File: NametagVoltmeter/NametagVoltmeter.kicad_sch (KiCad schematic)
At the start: 61 parts, among them J1 Conn_01x07_Pin, J11 I_Input, J12 Conn_01x02_Pin, J14 Barrel_Jack, J15 Barrel_Jack, J16 Conn_01x01_Socket, J17 Conn_01x01_Socket, J2 MicoSD, J3 Conn_01x07_Pin, J7 Conn_01x02_Pin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

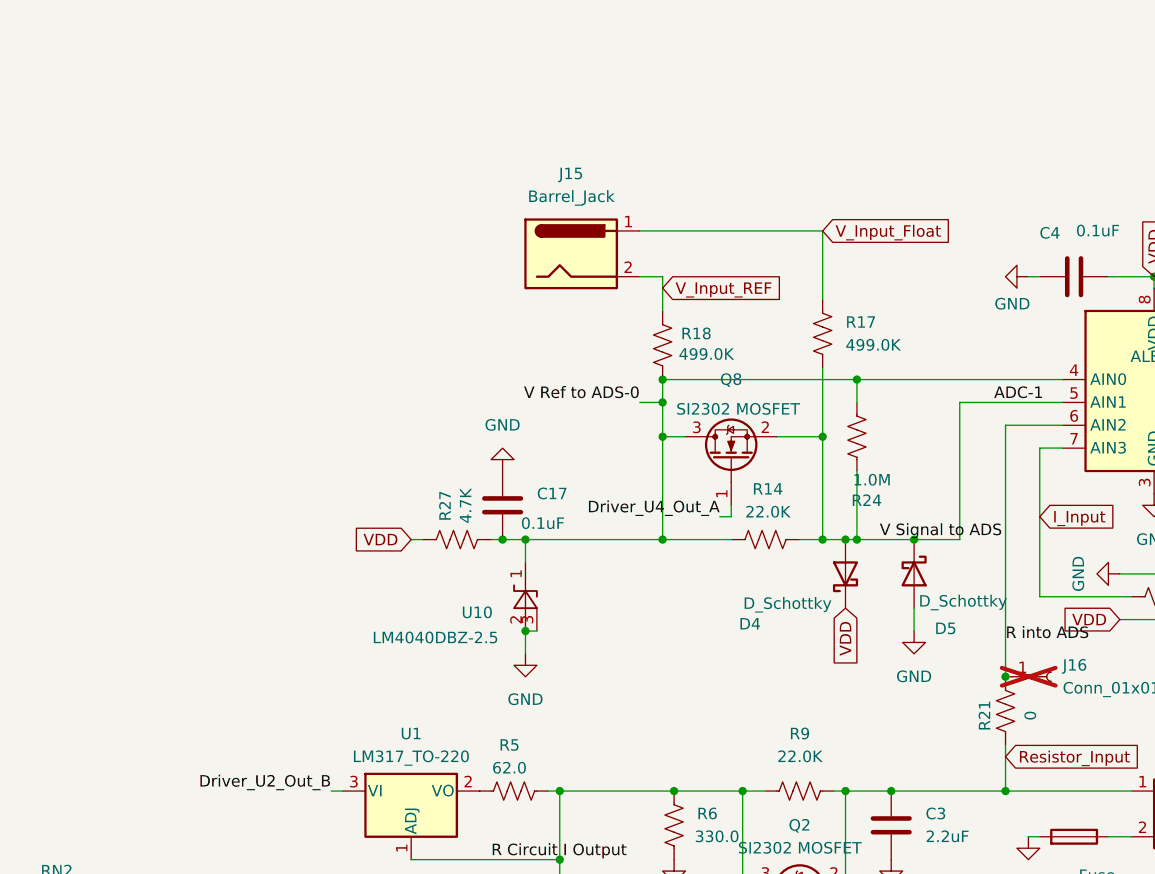
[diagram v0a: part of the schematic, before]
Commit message: Making a Version of Code for Newest PCB Revision
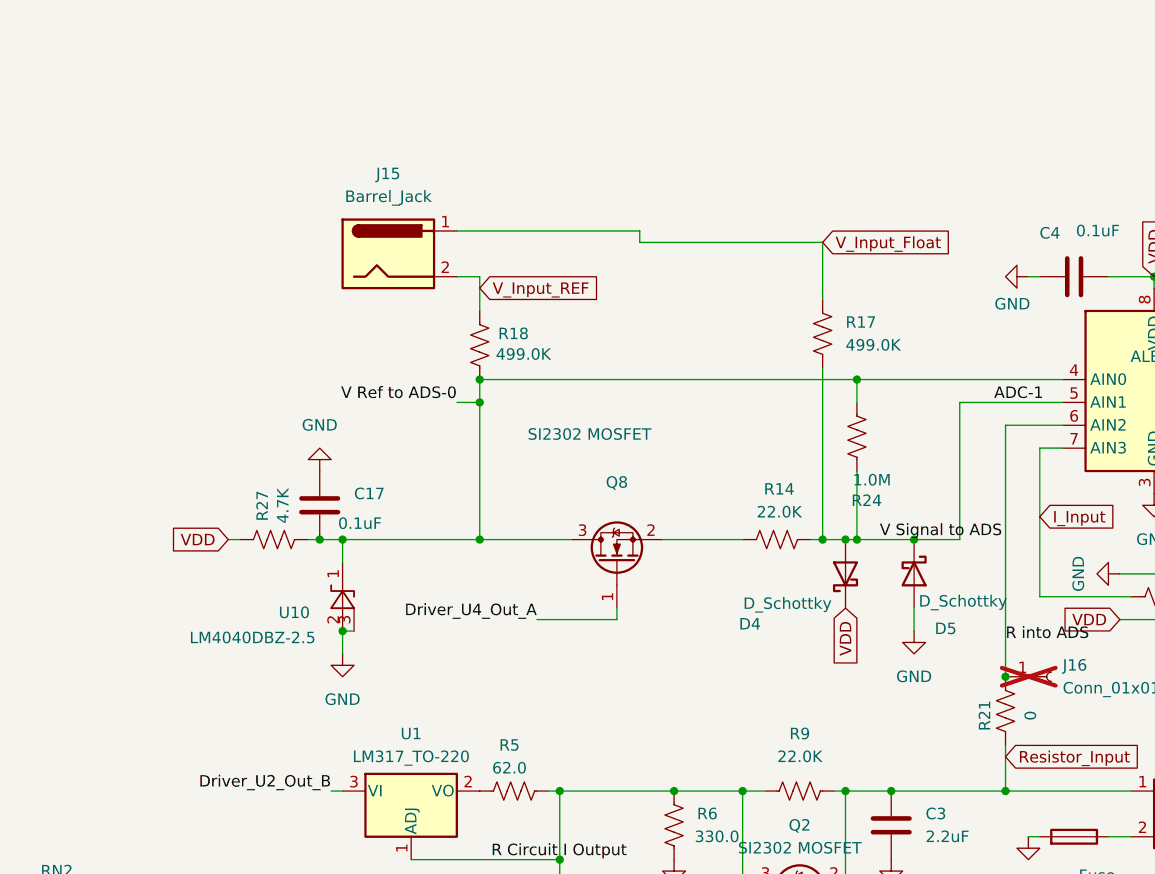
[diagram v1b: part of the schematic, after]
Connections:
- net ADC-1: no longer Q8.2 (S)
- net V Ref to ADS-0: no longer R14.1
- new net: Q8.2 (S), R14.1
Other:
- moved on the sheet: C17, J15, Q8, R14, R18, R27, U10

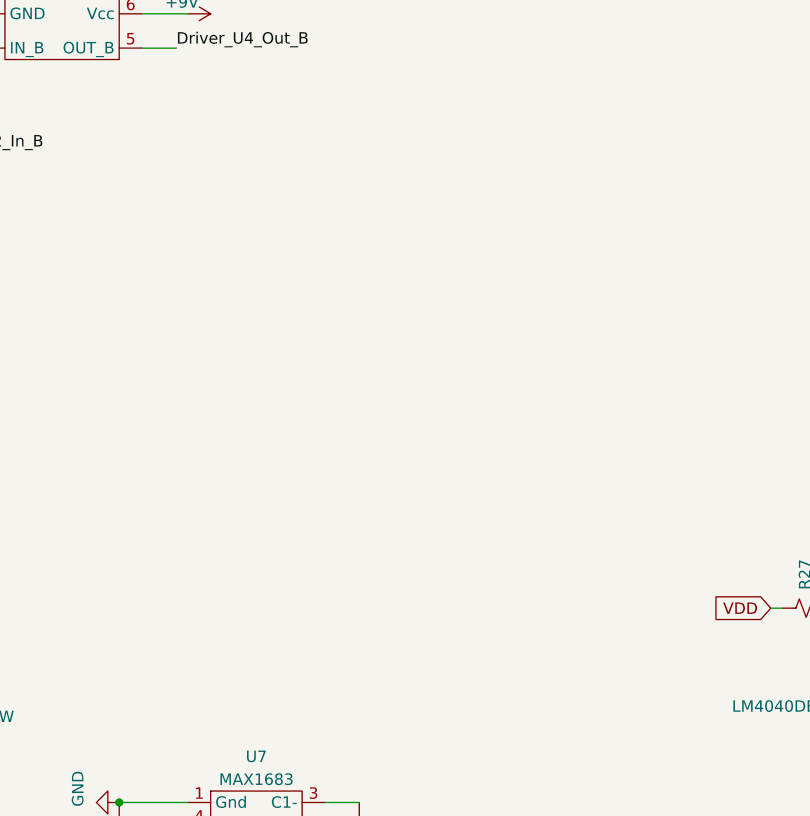
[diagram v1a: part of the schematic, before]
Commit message: Minor Giga Updates, Working on a business card size version
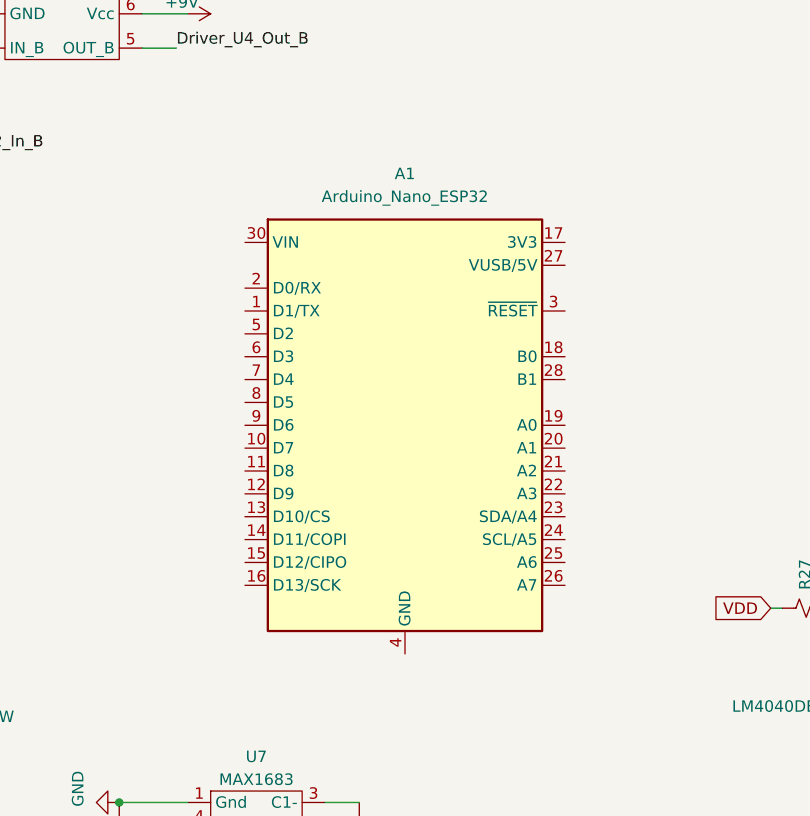
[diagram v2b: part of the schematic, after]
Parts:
- added A1: Arduino_Nano_ESP32, Module:Arduino_Nano, symbol MCU_Module:Arduino_Nano_ESP32
- RN1, RN2: footprint Resistor_SMD:R_Array_Convex_4x1206 -> Resistor_SMD:R_Array_Convex_4x0612
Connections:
- new net: A1.29 (GND), A1.4 (GND)
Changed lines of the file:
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@@
 			)
 		)
-		(property "Footprint" "Resistor_SMD:R_Array_Convex_4x1206"
+		(property "Footprint" "Resistor_SMD:R_Array_Convex_4x0612"
 			(at 274.955 57.15 90)
 			(effects
@@
 			)
 		)
-		(property "Footprint" "Resistor_SMD:R_Array_Convex_4x1206"
+		(property "Footprint" "Resistor_SMD:R_Array_Convex_4x0612"
 			(at 116.205 135.89 90)
 			(effects
@@
 					(unit 1)
 				)
+			)
+		)
+	)
+	(symbol
+		(lib_id "MCU_Module:Arduino_Nano_ESP32")
+		(at 77.47 69.85 0)
+		(unit 1)
+		(exclude_from_sim no)
+		(in_bom yes)
+		(on_board yes)
+		(dnp no)
+		(fields_autoplaced yes)
+		(property "Reference" "A1"
+			(at 77.47 41.91 0)
+			(effects
+				(font
+					(size 1.27 1.27)
+				)
+			)
+		)
+		(property "Value" "Arduino_Nano_ESP32"
+			(at 77.47 44.45 0)
+			(effects
+				(font
+					(size 1.27 1.27)
+				)
+			)
+		)
+		(property "Footprint" "Module:Arduino_Nano"
+			(at 91.186 103.886 0)
+			(effects
+				(font
+					(size 1.27 1.27)
+					(italic yes)
+				)
+				(hide yes)
+			)
+		)
+		(property "Datasheet" "https://docs.arduino.cc/resources/datasheets/ABX00083-datasheet.pdf"
+			(at 116.586 101.346 0)
+			(effects
+				(font
+					(size 1.27 1.27)
+				)
+				(hide yes)
+			)
+		)
+		(property "Description" "Arduino Nano board based on the ESP32-S3 with a dual-core 240 MHz processor, 384 kB ROM, 512 kB SRAM. Operates at 3.3V, with 5V USB-C® input and 6-21V VIN. Features Wi-Fi®, Bluetooth® LE, digital and analog pins, and supports SPI, I2C, UART, I2S, and CAN."
+			(at 215.9 98.806 0)
+			(effects
+				(font
+					(size 1.27 1.27)
+				)
+				(hide yes)
+			)
+		)
+		(pin "16"
+		)
+		(pin "27"
+		)
+		(pin "7"
+		)
+		(pin "12"
+		)
+		(pin "13"
+		)
+		(pin "19"
+		)
+		(pin "8"
+		)
+		(pin "30"
+		)
+		(pin "18"
+		)
+		(pin "11"
+		)
+		(pin "4"
+		)
+		(pin "14"
+		)
+		(pin "22"
+		)
+		(pin "17"
+		)
+		(pin "3"
+		)
+		(pin "24"
+		)
+		(pin "2"
+		)
+		(pin "9"
+		)
+		(pin "1"
+		)
+		(pin "5"
+		)
+		(pin "10"
+		)
+		(pin "15"
+		)
+		(pin "29"
+		)
+		(pin "6"
+		)
+		(pin "26"
+		)
+		(pin "28"
+		)
+		(pin "20"
+		)
+		(pin "23"
+		)
+		(pin "25"
+		)
+		(pin "21"
+		)
+		(instances
+			(project ""
+				(path "/39d8d4e4-ad86-4016-bf5f-66e0716621ab"
+					(reference "A1")
+					(unit 1)
+				)

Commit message: Working on next PCB, mostly.
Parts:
- added C1, C5, C6: 1uF, Capacitor_SMD:C_0805_2012Metric_Pad1.18x1.45mm_HandSolder, symbol Device:C
- added C2: 4.7uF, Capacitor_SMD:C_0805_2012Metric_Pad1.18x1.45mm_HandSolder, symbol Device:C
- added L2: 22uH, Inductor_SMD:L_Murata_DFE201610P, symbol Device:L
- added R10: 71.5k, Resistor_SMD:R_0805_2012Metric_Pad1.20x1.40mm_HandSolder, symbol Device:R_US
- added R8: 732k, Resistor_SMD:R_0805_2012Metric_Pad1.20x1.40mm_HandSolder, symbol Device:R_US
- added U5: TLV61046ADBVR, Package_TO_SOT_SMD:SOT-23-6_Handsoldering, symbol CustomLibrary:TLV61046ADBVR
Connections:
- net +3V3: now also A1.17 (3V3)
- net +9V: now also C2.1, R8.1, U5.5 (VOUT)
- net A0/D14: now also A1.19 (A0)
- net A1/D15: now also A1.20 (A1)
- net A2/D16: now also A1.21 (A2)
- net CLK: now also A1.16 (D13/SCK)
- net CS: now also A1.11 (D8)
- net D10~: now also A1.13 (D10/CS)
- net D3~: now also A1.6 (D3)
- net D5~ (IR): now also A1.8 (D5)
- net D6~: now also A1.9 (D6)
- net D7: now also A1.10 (D7)
- net D9~: now also A1.12 (D9)
- net GND: now also A1.29 (GND), A1.4 (GND), C1.2, C2.2, C5.2, C6.2, R10.2, U5.2 (GND)
- net MISO: now also A1.15 (D12/CIPO)
- net MOSI: now also A1.14 (D11/COPI)
- net SCL: now also A1.24 (SCL/A5)
- net SCL-5V: now also RN1.2 (R4.1); no longer RN1.3 (R3.1)
- net SDA: now also A1.23 (SDA/A4)
- net SDA-5V: now also RN1.3 (R3.1); no longer RN1.2 (R4.1)
- net VDD: now also L2.1, U5.6 (VIN)
- new net: C1.1, C5.1, C6.1, U5.4 (EN)
- new net: R10.1, R8.2, U5.3 (FB)
- new net: L2.2, U5.1 (SW)
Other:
- moved on the sheet: C10, C9, J2, Q6, Q7, RN2, U7

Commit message: Fixed ammeter problem and some nuisance alerts on Giga version
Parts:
- L2: footprint Inductor_SMD:L_Murata_DFE201610P -> Inductor_SMD:L_Taiyo-Yuden_MD-5050
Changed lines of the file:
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@@
 			)
 		)
-		(property "Footprint" "Inductor_SMD:L_Murata_DFE201610P"
+		(property "Footprint" "Inductor_SMD:L_Taiyo-Yuden_MD-5050"
 			(at -67.31 184.15 0)
 			(effects

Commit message: Edits to the RA4M1 version and KiCAD work
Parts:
- RN1, RN2: footprint Resistor_SMD:R_Array_Convex_4x0612 -> Library:RESCAXS127P508X320X70-8N
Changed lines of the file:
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@@
 			)
 		)
-		(property "Footprint" "Resistor_SMD:R_Array_Convex_4x0612"
+		(property "Footprint" "Library:RESCAXS127P508X320X70-8N"
 			(at 274.955 57.15 90)
 			(effects
@@
 			)
 		)
-		(property "Footprint" "Resistor_SMD:R_Array_Convex_4x0612"
+		(property "Footprint" "Library:RESCAXS127P508X320X70-8N"
 			(at 107.315 109.22 90)
 			(effects
